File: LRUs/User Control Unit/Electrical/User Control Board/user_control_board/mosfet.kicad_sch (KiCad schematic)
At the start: 3 parts, among them Q1 Q_PMOS_GDS

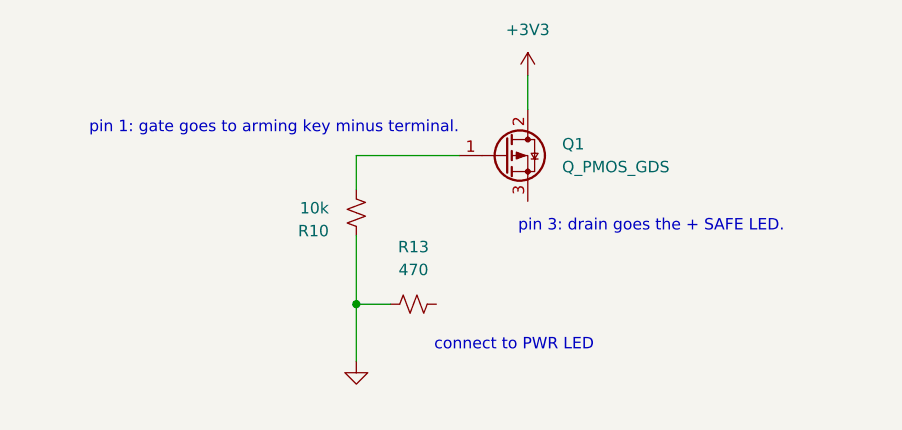
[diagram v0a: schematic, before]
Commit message: footprint and added symbol for audio
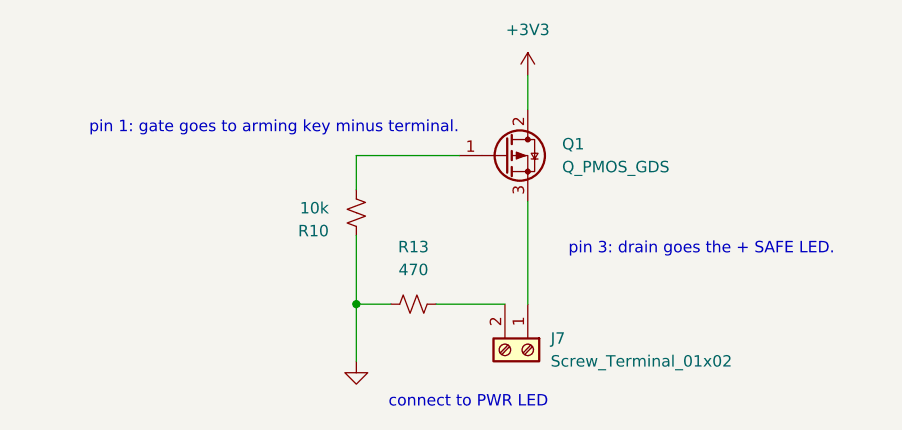
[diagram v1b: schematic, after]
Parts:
- added J7: Screw_Terminal_01x02, Package_SON:WSON-8-1EP_6x5mm_P1.27mm_EP3.4x4mm, symbol Connector:Screw_Terminal_01x02
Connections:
- net at R13.2: now also J7.2 (Pin_2)
- net at Q1.3 (S): now also J7.1 (Pin_1)
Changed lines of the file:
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@@
 	(text "connect to PWR LED\n"
 		(exclude_from_sim no)
-		(at 136.906 102.362 0)
+		(at 131.826 108.712 0)
 		(effects
 			(font
@@
 	(text "pin 3: drain goes the + SAFE LED.\n"
 		(exclude_from_sim no)
-		(at 152.146 89.154 0)
+		(at 157.734 91.694 0)
 		(effects
 			(font
@@
 		(pts
 			(xy 138.43 72.39) (xy 138.43 76.2)
+		)
+		(stroke
+			(width 0)
+			(type default)
+		)
+	)
+	(wire
+		(pts
+			(xy 128.27 97.79) (xy 135.89 97.79)
 		)
 		(stroke
@@
 	(wire
 		(pts
+			(xy 138.43 86.36) (xy 138.43 97.79)
+		)
+		(stroke
+			(width 0)
+			(type default)
+		)
+	)
+	(wire
+		(pts
 			(xy 119.38 81.28) (xy 119.38 85.09)
 		)
@@
 		)
 	)
+	(symbol
+		(lib_id "Connector:Screw_Terminal_01x02")
+		(at 138.43 102.87 270)
+		(unit 1)
+		(body_style 1)
+		(exclude_from_sim no)
+		(in_bom yes)
+		(on_board yes)
+		(in_pos_files yes)
+		(dnp no)
+		(fields_autoplaced yes)
+		(property "Reference" "J7"
+			(at 140.97 101.5999 90)
+			(show_name no)
+			(do_not_autoplace no)
+			(effects
+				(font
+					(size 1.27 1.27)
+				)
+				(justify left)
+			)
+		)
+		(property "Value" "Screw_Terminal_01x02"
+			(at 140.97 104.1399 90)
+			(show_name no)
+			(do_not_autoplace no)
+			(effects
+				(font
+					(size 1.27 1.27)
+				)
+				(justify left)
+			)
+		)
+		(property "Footprint" "Package_SON:WSON-8-1EP_6x5mm_P1.27mm_EP3.4x4mm"
+			(at 138.43 102.87 0)
+			(hide yes)
+			(show_name no)
+			(do_not_autoplace no)
+			(effects
+				(font
+					(size 1.27 1.27)
+				)
+			)
+		)
+		(property "Datasheet" ""
+			(at 138.43 102.87 0)
+			(hide yes)
+			(show_name no)
+			(do_not_autoplace no)
+			(effects
+				(font
+					(size 1.27 1.27)
+				)
+			)
+		)
+		(property "Description" "Generic screw terminal, single row, 01x02, script generated (kicad-library-utils/schlib/autogen/connector/)"
+			(at 138.43 102.87 0)
+			(hide yes)
+			(show_name no)
+			(do_not_autoplace no)
+			(effects
+				(font
+					(size 1.27 1.27)
+				)
+			)
+		)
+		(pin "2"
+		)
+		(pin "1"
+		)
+		(instances
+			(project "user_control_board"
+				(path "/0b01eee9-e8c8-4965-a431-95eb44ba626f"
+					(reference "J7")
+					(unit 1)
+				)
+			)
+		)
+	)
